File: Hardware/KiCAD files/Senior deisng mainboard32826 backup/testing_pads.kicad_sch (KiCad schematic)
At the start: 1 part, among them J21 Conn_02x10_Socket

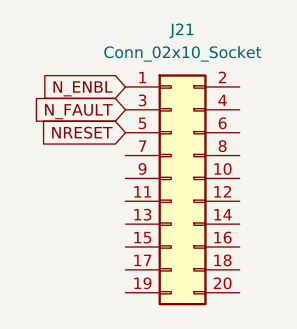
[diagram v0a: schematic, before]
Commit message: New project made to reflect layouts
New project files made in order to generate accurate layouts and create neatness.
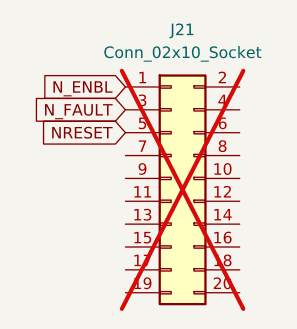
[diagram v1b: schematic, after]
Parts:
- J21: now not fitted
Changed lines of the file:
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@@
 		(on_board yes)
 		(in_pos_files yes)
-		(dnp no)
+		(dnp yes)
 		(fields_autoplaced yes)
 		(property "Reference" "J21"
